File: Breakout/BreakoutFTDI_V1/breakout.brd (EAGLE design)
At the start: 52.5 x 42.5 mm, 56 parts, among them Q1 16Mhz, U1 TPS63001DRCT, U11 XL

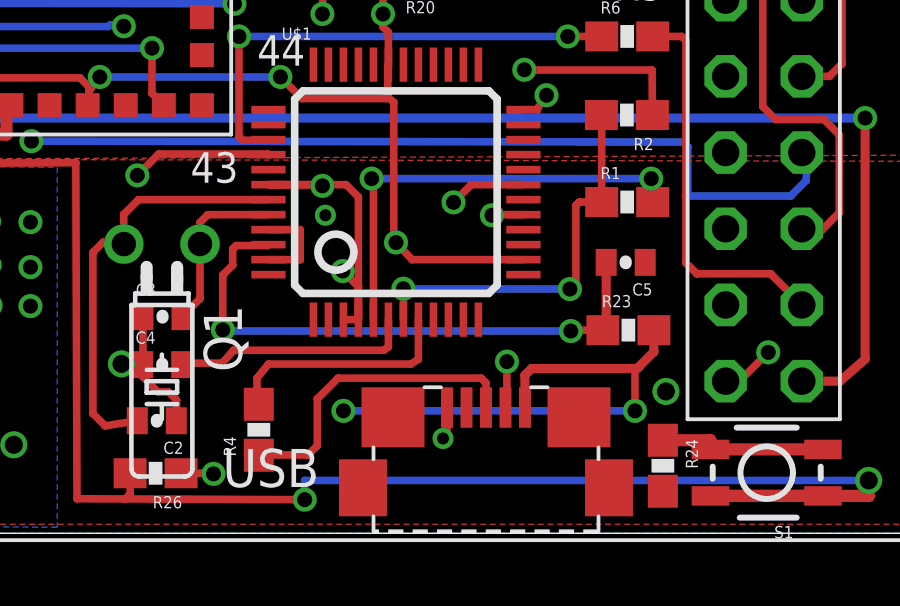
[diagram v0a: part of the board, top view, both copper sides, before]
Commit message: Added a Ferrite
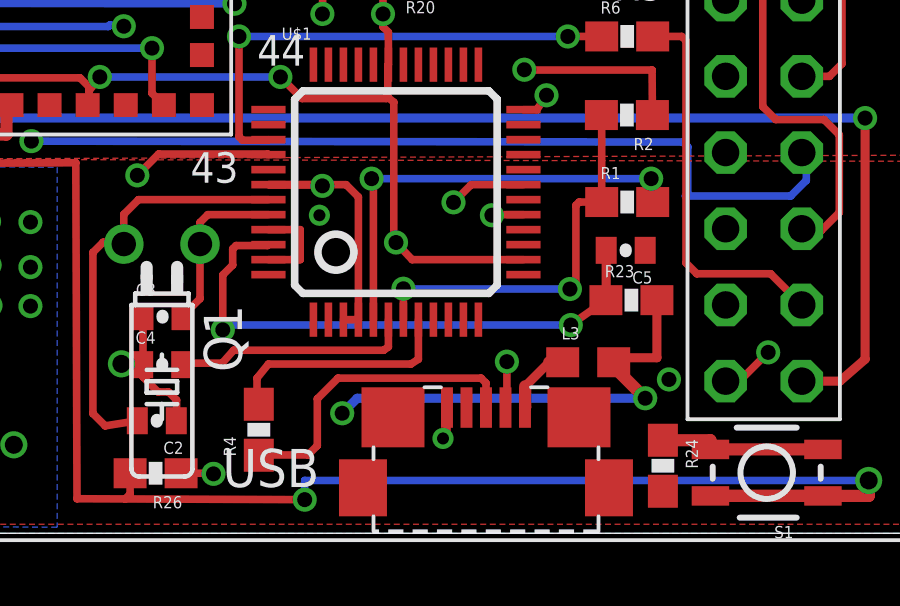
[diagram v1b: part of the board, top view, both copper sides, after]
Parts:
- added L3: (no value), Spark:0603
- moved R23 1.00 mm to (55.4, 7.77)
- moved C5 0.40 mm to (55.2, 9.43)
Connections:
- new net N$15: L3.1, USB.1
- net +5V_USB: now also L3.2; no longer USB.1
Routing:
- net N$15: track 0.00 -> 2.29 mm
- net +5V_USB: track 131.9 -> 131.2 mm, vias 8 -> 7
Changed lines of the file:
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@@
 <layers>
 <layer number="1" name="Top" color="4" fill="1" visible="yes" active="yes"/>
-<layer number="2" name="Route2" color="1" fill="3" visible="no" active="yes"/>
+<layer number="2" name="Route2" color="1" fill="3" visible="yes" active="yes"/>
 <layer number="3" name="Route3" color="4" fill="3" visible="no" active="no"/>
 <layer number="14" name="Route14" color="1" fill="6" visible="no" active="no"/>
-<layer number="15" name="Route15" color="4" fill="6" visible="no" active="yes"/>
-<layer number="16" name="Bottom" color="1" fill="1" visible="no" active="yes"/>
+<layer number="15" name="Route15" color="4" fill="6" visible="yes" active="yes"/>
+<layer number="16" name="Bottom" color="1" fill="1" visible="yes" active="yes"/>
 <layer number="17" name="Pads" color="2" fill="1" visible="yes" active="yes"/>
 <layer number="18" name="Vias" color="2" fill="1" visible="yes" active="yes"/>
@@
 <element name="R21" library="SparkFun-Resistors" package="0603-RES" value="33" x="51.57" y="18.48"/>
 <element name="R22" library="SparkFun-Resistors" package="0603-RES" value="33" x="44.22" y="18.47"/>
-<element name="R23" library="SparkFun-Resistors" package="0603-RES" value="470" x="55.34" y="6.77"/>
-<element name="C5" library="SparkFun-Passives" package="0402-CAP" value="0.1uF" x="55.25" y="9.03" rot="R180"/>
+<element name="R23" library="SparkFun-Resistors" package="0603-RES" value="470" x="55.44" y="7.77"/>
+<element name="C5" library="SparkFun-Passives" package="0402-CAP" value="0.1uF" x="55.25" y="9.43" rot="R180"/>
 <element name="S1" library="Spark" package="TACTILE_SWITCH_SMD" value="" x="59.95" y="2.02" rot="R180"/>
 <element name="R24" library="SparkFun-Resistors" package="0603-RES" value="33" x="56.49" y="2.25" rot="R270"/>
@@
 <element name="C10" library="SparkFun-Capacitors" package="0402-CAP" value=".1uF" x="47.62" y="34.7"/>
 <element name="R26" library="SparkFun-Resistors" package="0603-RES" value="100K" x="39.58" y="2" rot="R180"/>
+<element name="L3" library="Spark" package="0603" value="" x="54" y="5.7"/>
 </elements>
 <signals>
@@
 </polygon>
 <contactref element="R3" pad="2"/>
-<via x="56.5912" y="4.7264" extent="1-16" drill="0.6"/>
+<via x="56.6912" y="5.1264" extent="1-16" drill="0.5"/>
 <polygon width="0.254" layer="16">
 <vertex x="12" y="0"/>
@@
 <via x="21.898" y="38.5116" extent="1-16" drill="0.6"/>
 <via x="40.7934" y="31.4986" extent="1-16" drill="0.6"/>
-<via x="45.24" y="10.6" extent="1-16" drill="0.4"/>
+<via x="45.04" y="10.6" extent="1-16" drill="0.4"/>
 <wire x1="39.16" y1="5.63" x2="39.16" y2="5.21" width="0.254" layer="1"/>
 <wire x1="39.16" y1="5.21" x2="39.66" y2="4.71" width="0.254" layer="1"/>
@@
 <contactref element="U$2" pad="18"/>
 <contactref element="U$2" pad="19"/>
-<contactref element="USB" pad="1"/>
 <contactref element="R11" pad="2"/>
 <contactref element="R13" pad="2"/>
@@
 <wire x1="46.34" y1="11.21" x2="45.93" y2="11.62" width="0.254" layer="1"/>
 <wire x1="45.93" y1="11.62" x2="43.34" y2="11.62" width="0.254" layer="1"/>
-<wire x1="56.19" y1="6.77" x2="56.19" y2="6.05" width="0.3048" layer="1"/>
-<wire x1="56.19" y1="6.05" x2="55.695" y2="5.555" width="0.3048" layer="1"/>
-<wire x1="55.695" y1="5.555" x2="55.63" y2="5.49" width="0.3048" layer="1"/>
-<wire x1="55.63" y1="5.49" x2="52.11" y2="5.49" width="0.3048" layer="1"/>
-<wire x1="52.11" y1="5.49" x2="51.89" y2="5.27" width="0.3048" layer="1"/>
-<wire x1="51.89" y1="5.27" x2="51.89" y2="4.1928" width="0.3048" layer="1"/>
-<wire x1="51.89" y1="4.1928" x2="51.8928" y2="4.19" width="0.3048" layer="1"/>
+<wire x1="56.29" y1="7.77" x2="56.29" y2="5.85" width="0.3048" layer="1"/>
 <wire x1="27.7" y1="39.36" x2="30.01" y2="39.24" width="0.254" layer="1"/>
 <wire x1="30.01" y1="39.24" x2="30.29" y2="39.51" width="0.254" layer="1"/>
@@
 <wire x1="29.53" y1="38.71" x2="30.04" y2="38.71" width="0.254" layer="1"/>
 <wire x1="30.04" y1="38.71" x2="30.29" y2="39.51" width="0.254" layer="1"/>
-<wire x1="46.34" y1="7.12" x2="46.34" y2="8.22" width="0.254" layer="1"/>
-<wire x1="46.34" y1="8.22" x2="45.82" y2="8.74" width="0.254" layer="1"/>
-<via x="45.82" y="8.74" extent="1-16" drill="0.5"/>
-<wire x1="45.82" y1="8.74" x2="45.82" y2="4.15" width="0.254" layer="15"/>
-<wire x1="45.82" y1="4.15" x2="45.84" y2="4.08" width="0.254" layer="15"/>
-<via x="45.84" y="4.08" extent="1-16" drill="0.5"/>
-<wire x1="45.84" y1="4.08" x2="55.56" y2="4.08" width="0.254" layer="16"/>
-<via x="55.56" y="4.08" extent="1-16" drill="0.5"/>
-<wire x1="55.56" y1="4.08" x2="55.56" y2="5.42" width="0.254" layer="1"/>
-<wire x1="55.56" y1="5.42" x2="55.695" y2="5.555" width="0.254" layer="1"/>
 <wire x1="43.34" y1="11.62" x2="45.1" y2="11.62" width="0.254" layer="1"/>
 <wire x1="45.1" y1="11.62" x2="45.14" y2="11.58" width="0.254" layer="1"/>
@@
 <wire x1="16.1" y1="35.12" x2="16.06" y2="34.99" width="0.254" layer="16"/>
 <via x="16.06" y="34.99" extent="1-16" drill="0.5"/>
+<contactref element="L3" pad="2"/>
+<wire x1="56.29" y1="5.85" x2="55" y2="5.85" width="0.3048" layer="1"/>
+<wire x1="55" y1="5.85" x2="54.85" y2="5.7" width="0.4064" layer="1"/>
+<wire x1="54.85" y1="5.7" x2="54.85" y2="5.55" width="0.4064" layer="1"/>
+<wire x1="54.85" y1="5.55" x2="55.9" y2="4.5" width="0.4064" layer="1"/>
+<via x="55.9" y="4.5" extent="1-16" drill="0.5"/>
+<wire x1="55.9" y1="4.5" x2="46.3" y2="4.5" width="0.3048" layer="16"/>
+<wire x1="46.3" y1="4.5" x2="45.8" y2="4" width="0.3048" layer="16"/>
+<via x="45.8" y="4" extent="1-16" drill="0.5"/>
+<wire x1="45.14" y1="11.58" x2="45.42" y2="11.58" width="0.3048" layer="2"/>
+<wire x1="45.42" y1="11.58" x2="45.9" y2="11.1" width="0.3048" layer="2"/>
+<wire x1="45.9" y1="11.1" x2="45.9" y2="4.1" width="0.3048" layer="2"/>
+<wire x1="45.9" y1="4.1" x2="45.8" y2="4" width="0.3048" layer="2"/>
 </signal>
 <signal name="N$17">
@@
 <contactref element="R23" pad="1"/>
 <contactref element="C5" pad="2"/>
-<wire x1="54.6" y1="9.03" x2="54.6" y2="6.88" width="0.3048" layer="1"/>
-<wire x1="54.6" y1="6.88" x2="54.49" y2="6.77" width="0.3048" layer="1"/>
-<wire x1="54.49" y1="6.77" x2="53.45" y2="6.77" width="0.254" layer="1"/>
-<wire x1="53.45" y1="6.77" x2="53.42" y2="6.74" width="0.254" layer="1"/>
-<via x="53.42" y="6.74" extent="1-16" drill="0.5"/>
-<wire x1="53.42" y1="6.74" x2="41.86" y2="6.74" width="0.254" layer="16"/>
-<wire x1="41.86" y1="6.74" x2="41.82" y2="6.78" width="0.254" layer="16"/>
+<wire x1="54.6" y1="9.43" x2="54.6" y2="7.78" width="0.3048" layer="1"/>
+<wire x1="54.6" y1="7.78" x2="54.59" y2="7.77" width="0.3048" layer="1"/>
+<wire x1="54.59" y1="7.77" x2="53.45" y2="6.97" width="0.254" layer="1"/>
+<wire x1="53.45" y1="6.97" x2="53.42" y2="6.94" width="0.254" layer="1"/>
+<via x="53.42" y="6.94" extent="1-16" drill="0.5"/>
+<wire x1="53.42" y1="6.94" x2="41.86" y2="6.94" width="0.254" layer="16"/>
+<wire x1="41.86" y1="6.94" x2="41.82" y2="6.78" width="0.254" layer="16"/>
 <via x="41.82" y="6.78" extent="1-16" drill="0.5"/>
 <wire x1="41.82" y1="6.78" x2="41.82" y2="8.61" width="0.254" layer="1"/>
@@
 <wire x1="37.25" y1="30.82" x2="37.25" y2="31.34" width="0.254" layer="16"/>
 </signal>
+<signal name="N$15">
+<contactref element="USB" pad="1"/>
+<contactref element="L3" pad="1"/>
+<wire x1="53.15" y1="5.7" x2="52.7" y2="5.7" width="0.4064" layer="1"/>
+<wire x1="52.7" y1="5.7" x2="51.9" y2="4.9" width="0.3048" layer="1"/>
+<wire x1="51.9" y1="4.9" x2="51.9" y2="4.1972" width="0.4064" layer="1"/>
+<wire x1="51.9" y1="4.1972" x2="51.8928" y2="4.19" width="0.4064" layer="1"/>
+</signal>
 </signals>
